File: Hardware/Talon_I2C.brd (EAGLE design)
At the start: 140 x 19 mm, 93 parts, among them J1 CONN_TALON_REMOTE, J2 CONN_I2C_LOGGER, J3 CONN_I2C_LOGGER, J4 CONN_I2C_LOGGER, J5 CONN_I2C_LOGGER, Q1 2N7002, Q2 2N7002, Q3 2N7002, Q4 2N7002, Q5 AO3419, Q6 AO3419, Q7 AO3419, Q8 AO3419, U1 SN74HC04, U10 74HC4852, U11 SN74LVC1G3157SC70, U12 MCP3421A3, U13 FXMAR2102UMLP, U14 PCA9617WSON, U15 PCA9617WSON, U16 PCA9617WSON, U17 PCA9617WSON, U18 SN74AUP1G08DCK, U19 SN74AUP1G08DCK, U2 CD4044, U20 SN74AUP1G08DCK, U21 SN74AUP1G08DCK, U3 SIP32431TDFN, U4 INA4180A2, U5 MAX9034TSSOP, U6 SN74AC08, U7 24AA02SOT23, U8 MCP23018QFN, U9 PCA9536DFN

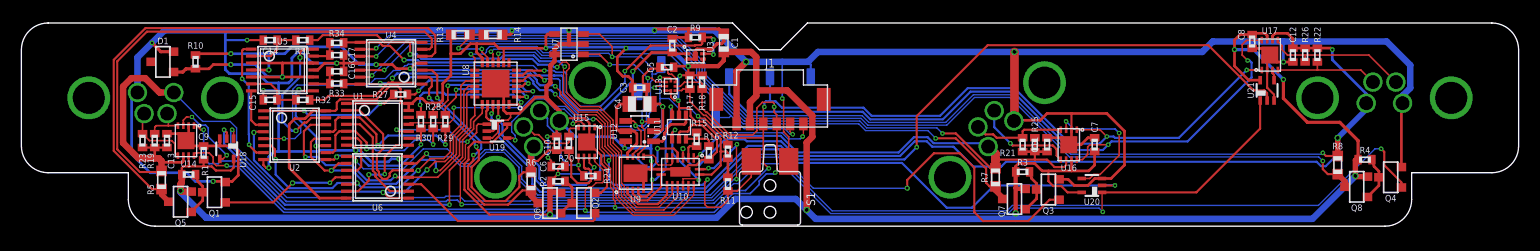
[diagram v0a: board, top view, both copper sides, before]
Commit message: v1.1 updates
Moved port 1 and port 4, sent to fab
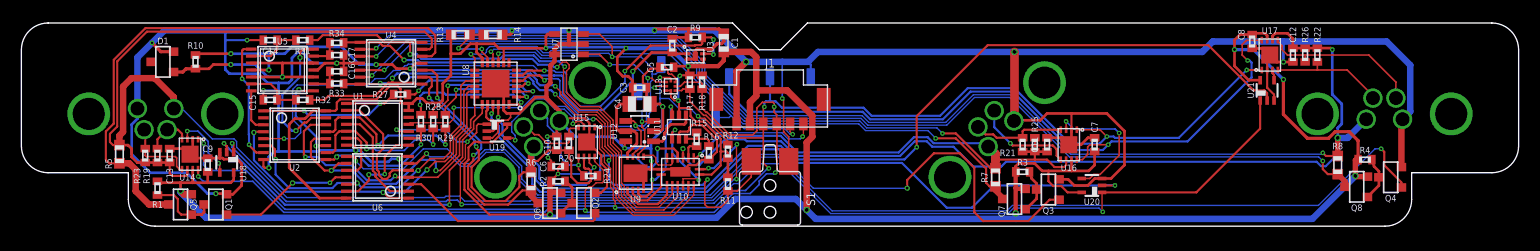
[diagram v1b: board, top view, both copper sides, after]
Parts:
- moved R5 4.62 mm to (-60.8, 6.73)
- moved R1 3.19 mm to (-57.3, 3.56), turned to 90 degrees
- moved J2 1.50 mm to (-57.5, 10.5)
- moved J5 1.50 mm to (57.5, 10.5)
- moved C13 1.42 mm to (-56.1, 6.60)
- moved R19 1.42 mm to (-57.3, 6.60)
- moved R23 1.42 mm to (-58.4, 6.60)
- moved U14 1.33 mm to (-54.2, 6.73)
- moved U18 1.27 mm to (-50.8, 5.97)
- moved C9 1.20 mm to (-52.6, 5.71)
- moved Q1 1.15 mm to (-51.8, 2.03)
- moved Q5 0.25 mm to (-55.1, 2.03)
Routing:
- net VPORT1_OUT: track 134.6 -> 128.3 mm
- net N$2: track 4.16 -> 7.00 mm
- net 3V3: track 338.7 -> 341.3 mm
- net SENSE1+: track 50.5 -> 53.0 mm
- net !I2C_OB_EN: track 129.8 -> 127.9 mm
- net PORT4_SCL: track 13.6 -> 15.1 mm
- net VPORT4_OUT: track 187.7 -> 189.2 mm
- net SDA: track 144.9 -> 143.5 mm
- net DATA1_EN: track 36.3 -> 35.1 mm
- net SCL: track 155.3 -> 154.2 mm
- net DATA1_EN_LOCAL: track 7.45 -> 6.47 mm
- net PORT4_SDA: track 10.1 -> 10.9 mm
- net GND: track 386.2 -> 386.7 mm
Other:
- board text added: "Talon - I2C v1.1 Bobby Schulz"
- board text removed: "Talon - I2C v1.0 Bobby Schulz"
